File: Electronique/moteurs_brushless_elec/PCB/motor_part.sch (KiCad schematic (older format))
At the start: 36 parts, among them K1 Maxon-200142, K2 Maxon-200142, U1 L6235D, U2 L6235D

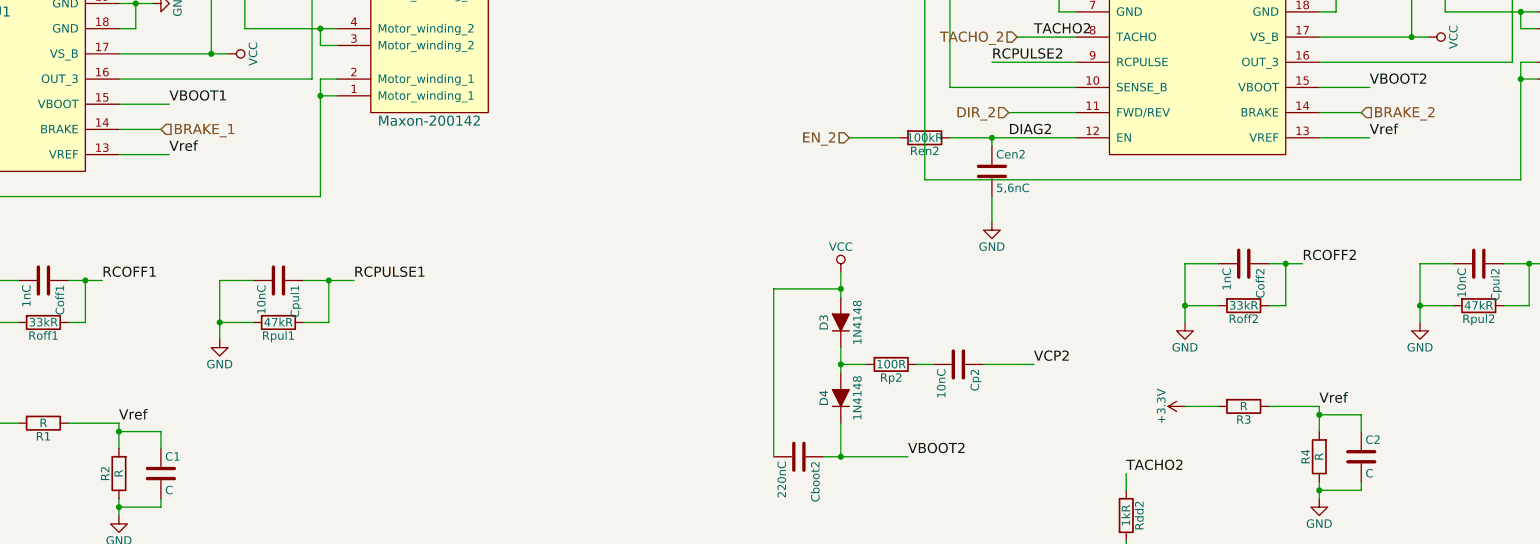
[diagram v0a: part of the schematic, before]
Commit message: placement brushless
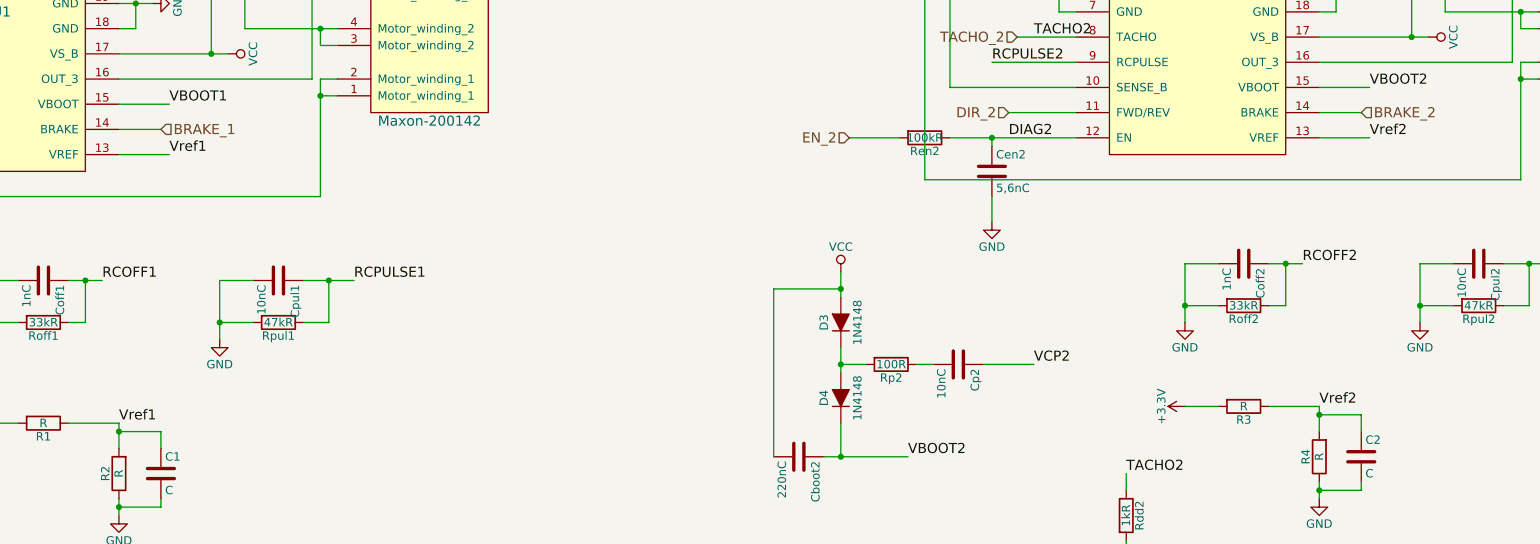
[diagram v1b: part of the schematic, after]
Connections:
- net Vref renamed Vref1
- net Vref1: no longer C2.1, R3.1, R4.2, U2.13 (VREF)
- new net Vref2: C2.1, R3.1, R4.2, U2.13 (VREF)
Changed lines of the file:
@@
 	3150 3050 3550 3050
 Text Label 5300 3200 0    60   ~ 0
-Vref
+Vref1
 Wire Wire Line
 	5000 3200 5300 3200
 Text Label 5000 4800 0    60   ~ 0
-Vref
+Vref1
 $Comp
 L R R1
@@
 	10300 2950 10700 2950
 Text Label 12450 3100 0    60   ~ 0
-Vref
+Vref2
 Wire Wire Line
 	12150 3100 12450 3100
 Text Label 12150 4700 0    60   ~ 0
-Vref
+Vref2
 $Comp
 L R R3

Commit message: rectification des empreintes
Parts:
- D1, D2, D3, D4: footprint Diodes_SMD:D_SOD-123 -> Diodes_THT:D_DO-35_SOD27_P10.16mm_Horizontal
- K1, K2: footprint maxon:Molex-52207-0433 -> maxon:Molex-52610-1133
- R1, R2, R3, R4: footprint Resistors_SMD:R_1206_HandSoldering -> Resistors_THT:R_Axial_DIN0207_L6.3mm_D2.5mm_P10.16mm_Horizontal
- Rsense1, Rsense2: footprint Resistors_THT:R_Axial_DIN0414_L11.9mm_D4.5mm_P20.32mm_Horizontal -> Resistors_THT:R_Bare_Metal_Element_L12.4mm_W4.8mm_P11.40mm
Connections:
- net VCC: no longer Cboot2.2, D3.2 (A), U2.17 (VS_B), U2.20 (VS_A)
- new net VDD: Cboot2.2, D3.2 (A), U2.17 (VS_B), U2.20 (VS_A)
